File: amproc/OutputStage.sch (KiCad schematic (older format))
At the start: 22 parts, among them J1 OUT, Q5 BC546, Q6 BC556, U6 TL072, U7 TL072

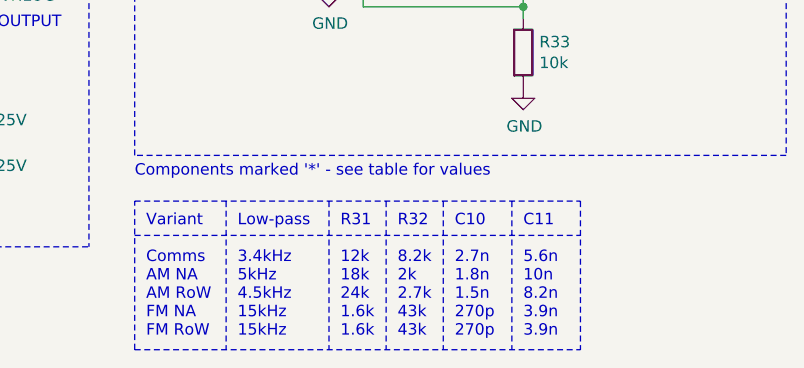
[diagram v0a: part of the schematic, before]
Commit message: Changed LPF, pre-emphasis component values in AM (NA and RoW) variants to correct bandwidth
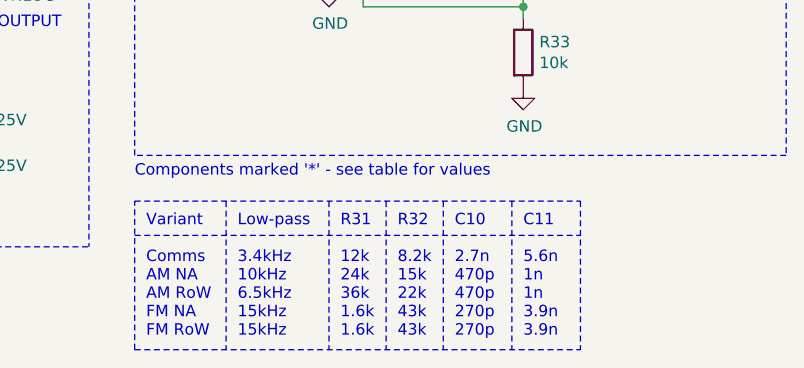
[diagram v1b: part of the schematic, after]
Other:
- note added: "C10\n\n2.7n\n470p\n470p\n270p\n270p"
- note added: "C11\n\n5.6n\n1n\n1n\n3.9n\n3.9n"
- note added: "Low-pass\n\n3.4kHz\n10kHz\n6.5kHz\n15kHz\n15kHz"
- note added: "R31\n\n12k\n24k\n36k\n1.6k\n1.6k"
- note added: "R32\n\n8.2k\n15k\n22k\n43k\n43k"
- note removed: "C10\n\n2.7n\n1.8n\n1.5n\n270p\n270p"
- note removed: "C11\n\n5.6n\n10n\n8.2n\n3.9n\n3.9n"
- note removed: "Low-pass\n\n3.4kHz\n5kHz\n4.5kHz\n15kHz\n15kHz"
- note removed: "R31\n\n12k\n18k\n24k\n1.6k\n1.6k"
- note removed: "R32\n\n8.2k\n2k\n2.7k\n43k\n43k"
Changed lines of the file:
@@
 	8650 2600 8650 2700
 Connection ~ 8650 2700
-Text Notes 7400 4950 0    50   ~ 0
-Low-pass\n\n3.4kHz\n5kHz\n4.5kHz\n15kHz\n15kHz
-Text Notes 7850 4950 0    50   ~ 0
-R31\n\n12k\n18k\n24k\n1.6k\n1.6k
-Text Notes 8100 4950 0    50   ~ 0
-R32\n\n8.2k\n2k\n2.7k\n43k\n43k
-Text Notes 8350 4950 0    50   ~ 0
-C10\n\n2.7n\n1.8n\n1.5n\n270p\n270p
-Text Notes 8650 4950 0    50   ~ 0
-C11\n\n5.6n\n10n\n8.2n\n3.9n\n3.9n
 Wire Notes Line style solid
 	7350 4350 7350 5000
@@
 Wire Notes Line
 	5250 2350 5250 4550
+Text Notes 7400 4950 0    50   ~ 0
+Low-pass\n\n3.4kHz\n10kHz\n6.5kHz\n15kHz\n15kHz
+Text Notes 8100 4950 0    50   ~ 0
+R32\n\n8.2k\n15k\n22k\n43k\n43k
+Text Notes 8350 4950 0    50   ~ 0
+C10\n\n2.7n\n470p\n470p\n270p\n270p
+Text Notes 8650 4950 0    50   ~ 0
+C11\n\n5.6n\n1n\n1n\n3.9n\n3.9n
+Text Notes 7850 4950 0    50   ~ 0
+R31\n\n12k\n24k\n36k\n1.6k\n1.6k
 $EndSCHEMATC
